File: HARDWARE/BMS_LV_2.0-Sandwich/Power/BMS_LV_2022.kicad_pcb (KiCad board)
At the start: 4 copper layers, 90 x 45 mm, 121 parts, among them J1 Conn_01x26, J11 Conn_01x07_Female, J2 AS214-97PN, J4 Battery+, J5 Battery-, J6 Conn_01x09_Female, Q1 BC846, Q10 BSS138, Q12 SIR5607DP-T1-RE3, Q13 SIR5607DP-T1-RE3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

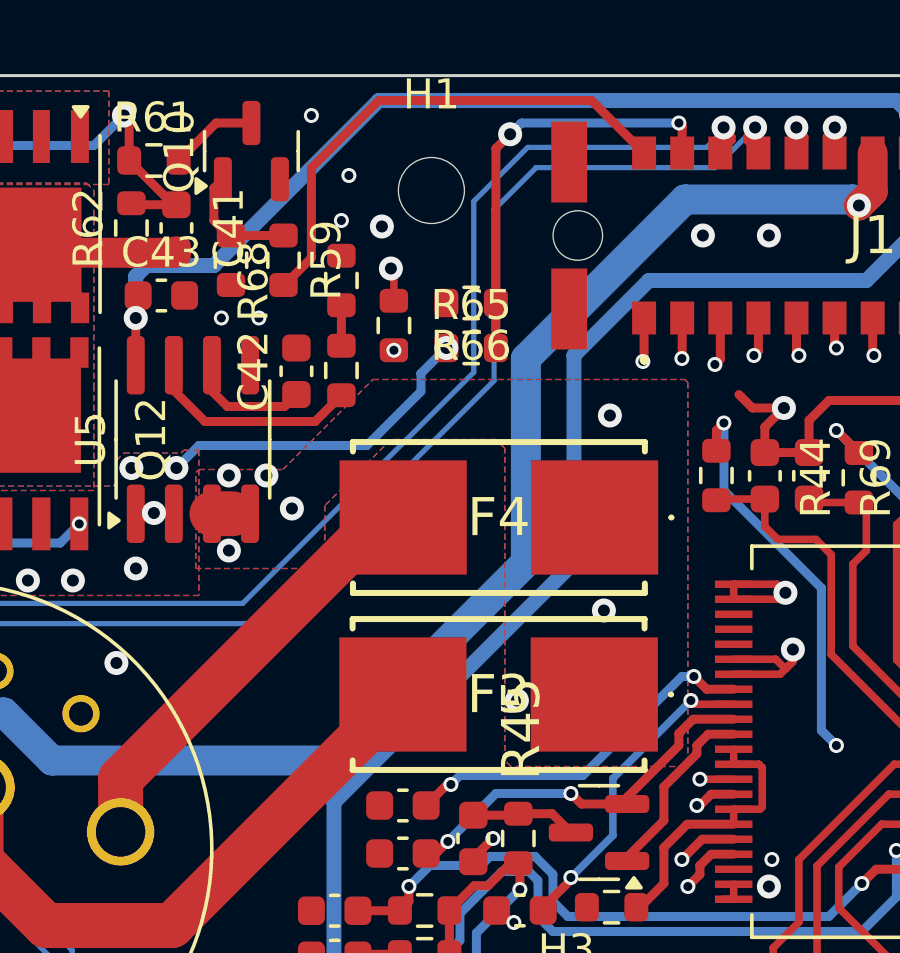
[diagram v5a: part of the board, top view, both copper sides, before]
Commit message: Przesunięto złącze do thermistorów oraz programator aby nie bylo kolizji, przesunięto tez bezpieczniki
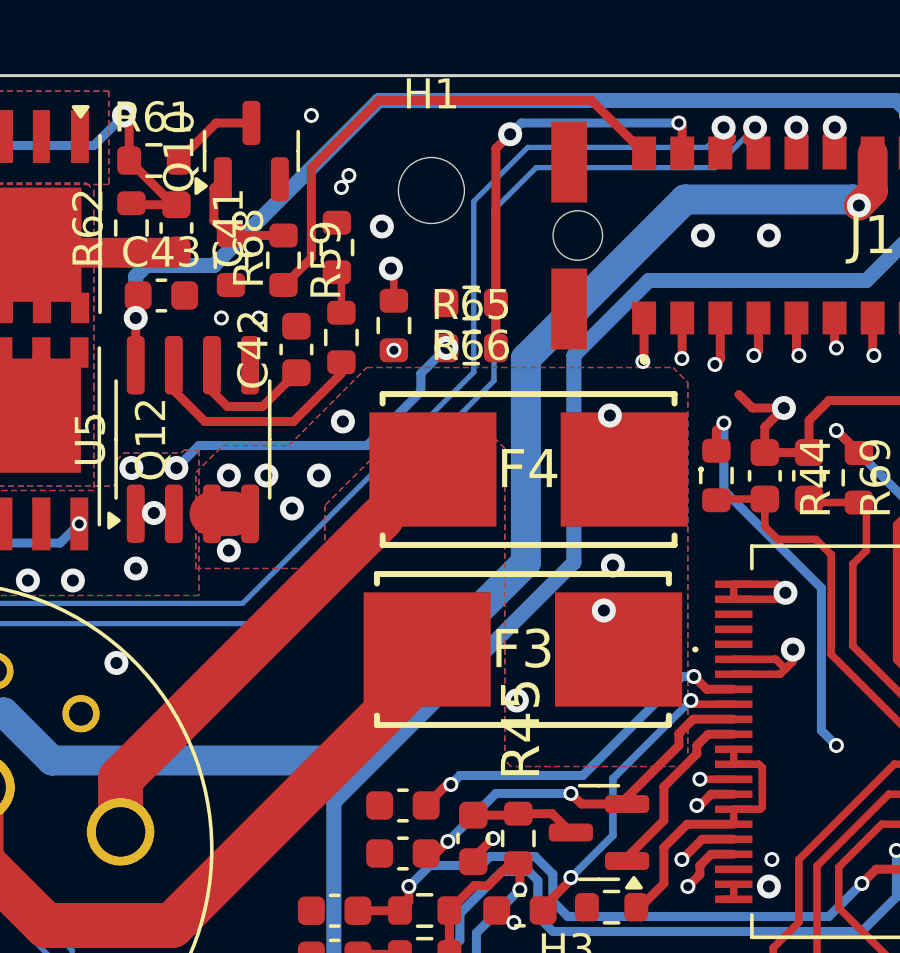
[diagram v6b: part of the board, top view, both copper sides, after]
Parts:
- moved F4 1.88 mm to (144.7, 93.1)
- moved F3 1.70 mm to (144.5, 99.1)
- moved R68 1.11 mm to (138.3, 85.7)
- moved R67 1.10 mm to (138.5, 88.7)
- moved C42 0.73 mm to (137.0, 89.1)
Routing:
- net Net-(J2-PadH): track 31.7 -> 31.0 mm
- net Net-(F3-Pad1): vias 7 -> 10
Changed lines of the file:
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@@
 	(footprint "Capacitor_SMD:C_0603_1608Metric"
 		(layer "F.Cu")
-		(at 136.967903 89.855 90)
+		(at 136.967903 89.13 90)
 		(descr "Capacitor SMD 0603 (1608 Metric), square (rectangular) end terminal, IPC-7351 nominal, (Body size source: IPC-SM-782 page 76, https://www.pcb-3d.com/wordpress/wp-content/uploads/ipc-sm-782a_amendment_1_and_2.pdf), generated with kicad-footprint-generator")
 		(tags "capacitor")
@@
 	(footprint "footprints:01550900DR"
 		(layer "F.Cu")
-		(at 143.717903 94.73 180)
+		(at 144.707903 93.13 180)
 		(descr "01550900DR-2")
 		(tags "Fuse")
@@
 	(footprint "Resistor_SMD:R_0603_1608Metric"
 		(layer "F.Cu")
-		(at 138.467903 86.83 90)
+		(at 138.317903 85.73 90)
 		(descr "Resistor SMD 0603 (1608 Metric), square (rectangular) end terminal, IPC-7351 nominal, (Body size source: IPC-SM-782 page 72, https://www.pcb-3d.com/wordpress/wp-content/uploads/ipc-sm-782a_amendment_1_and_2.pdf), generated with kicad-footprint-generator")
 		(tags "resistor")
@@
 	(footprint "footprints:01550900DR"
 		(layer "F.Cu")
-		(at 143.707904 100.63 180)
+		(at 144.517903 99.13 180)
 		(descr "01550900DR-2")
 		(tags "Fuse")
@@
 	(footprint "Resistor_SMD:R_0603_1608Metric"
 		(layer "F.Cu")
-		(at 138.467903 89.83 90)
+		(at 138.467903 88.73 90)
 		(descr "Resistor SMD 0603 (1608 Metric), square (rectangular) end terminal, IPC-7351 nominal, (Body size source: IPC-SM-782 page 72, https://www.pcb-3d.com/wordpress/wp-content/uploads/ipc-sm-782a_amendment_1_and_2.pdf), generated with kicad-footprint-generator")
 		(tags "resistor")
@@
 	)
 	(via
-		(at 138.467903 84.83)
+		(at 138.467903 83.73)
 		(size 0.5)
 		(drill 0.3)
@@
 	)
 	(segment
-		(start 136.967903 90.63)
-		(end 136.567903 91.03)
+		(start 134.667903 91.03)
+		(end 135.842903 91.03)
 		(width 0.3)
 		(layer "F.Cu")
@@
 	)
 	(segment
-		(start 134.667903 91.03)
-		(end 134.152903 90.515)
+		(start 135.842903 91.03)
+		(end 136.967903 89.905)
 		(width 0.3)
 		(layer "F.Cu")
@@
 	)
 	(segment
-		(start 134.152903 90.515)
-		(end 134.152903 89.655)
+		(start 134.152903 89.655)
+		(end 134.152903 90.515)
 		(width 0.3)
 		(layer "F.Cu")
@@
 	)
 	(segment
-		(start 136.567903 91.03)
+		(start 134.152903 90.515)
 		(end 134.667903 91.03)
 		(width 0.3)
@@
 	)
 	(via
+		(at 137.717903 93.33)
+		(size 0.8)
+		(drill 0.4)
+		(layers "F.Cu" "B.Cu")
+		(free yes)
+		(net 47)
+	)
+	(via
+		(at 138.517903 91.53)
+		(size 0.8)
+		(drill 0.4)
+		(layers "F.Cu" "B.Cu")
+		(free yes)
+		(net 47)
+	)
+	(via
 		(at 136.817903 94.43)
 		(size 0.8)
@@
 	)
 	(via
+		(at 147.517903 96.33)
+		(size 0.8)
+		(drill 0.4)
+		(layers "F.Cu" "B.Cu")
+		(free yes)
+		(net 47)
+	)
+	(via
 		(at 134.717903 93.33)
 		(size 0.8)
@@
 	)
 	(segment
-		(start 137.467903 86.08)
-		(end 136.567903 86.98)
+		(start 139.717903 80.83)
+		(end 137.467903 83.08)
 		(width 0.3)
 		(layer "F.Cu")
@@
 	)
 	(segment
-		(start 146.807903 80.83)
-		(end 139.717903 80.83)
+		(start 137.467903 83.08)
+		(end 137.467903 86.08)
 		(width 0.3)
 		(layer "F.Cu")
@@
 	)
 	(segment
-		(start 137.467903 83.08)
-		(end 137.467903 86.08)
+		(start 146.807903 80.83)
+		(end 139.717903 80.83)
 		(width 0.3)
 		(layer "F.Cu")
@@
 	)
 	(segment
-		(start 139.717903 80.83)
-		(end 137.467903 83.08)
+		(start 137.467903 86.08)
+		(end 136.567903 86.98)
 		(width 0.3)
 		(layer "F.Cu")
@@
 	)
 	(segment
-		(start 132.882903 90.495)
-		(end 133.917903 91.53)
+		(start 132.882903 89.655)
+		(end 132.882903 90.495)
 		(width 0.3)
 		(layer "F.Cu")
@@
 	)
 	(segment
-		(start 137.592903 91.53)
-		(end 138.467903 90.655)
+		(start 133.917903 91.53)
+		(end 136.867903 91.53)
 		(width 0.3)
 		(layer "F.Cu")
@@
 	)
 	(segment
-		(start 133.917903 91.53)
-		(end 137.592903 91.53)
+		(start 136.867903 91.53)
+		(end 138.467903 89.93)
 		(width 0.3)
 		(layer "F.Cu")
@@
 	)
 	(segment
-		(start 132.882903 89.655)
-		(end 132.882903 90.495)
+		(start 132.882903 90.495)
+		(end 133.917903 91.53)
 		(width 0.3)
 		(layer "F.Cu")
@@
 	)
 	(segment
-		(start 138.467903 87.655)
-		(end 138.467903 89.005)
-		(width 0.3)
+		(start 138.467903 86.705)
+		(end 138.317903 86.555)
+		(width 0.25)
+		(layer "F.Cu")
+		(net 66)
+	)
+	(segment
+		(start 138.467903 87.905)
+		(end 138.467903 86.705)
+		(width 0.25)
 		(layer "F.Cu")
 		(net 66)
@@
 	)
 	(segment
-		(start 124.517903 101.13)
-		(end 122.417903 103.23)
-		(width 0.3)
-		(layer "In2.Cu")
-		(net 81)
-	)
-	(segment
-		(start 131.317903 97.33)
-		(end 127.517903 101.13)
-		(width 0.3)
-		(layer "In2.Cu")
-		(net 81)
-	)
-	(segment
-		(start 134.467903 92.08)
-		(end 133.717903 92.83)
+		(start 122.417903 103.23)
+		(end 122.417903 105.33)
 		(width 0.3)
 		(layer "In2.Cu")
@@
 	)
 	(segment
-		(start 127.517903 101.13)
-		(end 124.517903 101.13)
+		(start 140.217903 89.155)
+		(end 137.392903 89.155)
 		(width 0.3)
 		(layer "In2.Cu")
@@
 	)
 	(segment
-		(start 140.217903 90.33)
-		(end 138.467903 92.08)
+		(start 122.417903 105.33)
+		(end 120.307903 107.44)
 		(width 0.3)
 		(layer "In2.Cu")
@@
 	)
 	(segment
-		(start 122.417903 105.33)
-		(end 120.307903 107.44)
+		(start 132.217903 97.33)
+		(end 131.317903 97.33)
 		(width 0.3)
 		(layer "In2.Cu")
@@
 	)
 	(segment
-		(start 133.717903 92.83)
-		(end 133.717903 95.83)
+		(start 120.307903 107.44)
+		(end 119.763208 107.44)
 		(width 0.3)
 		(layer "In2.Cu")
@@
 	)
 	(segment
-		(start 133.717903 95.83)
-		(end 132.217903 97.33)
+		(start 124.517903 101.13)
+		(end 122.417903 103.23)
 		(width 0.3)
 		(layer "In2.Cu")
@@
 	)
 	(segment
-		(start 140.217903 89.155)
-		(end 140.217903 90.33)
+		(start 127.517903 101.13)
+		(end 124.517903 101.13)
 		(width 0.3)
 		(layer "In2.Cu")
@@
 	)
 	(segment
-		(start 138.467903 92.08)
-		(end 134.467903 92.08)
+		(start 137.392903 89.155)
+		(end 133.717903 92.83)
 		(width 0.3)
 		(layer "In2.Cu")
@@
 	)
 	(segment
-		(start 122.417903 103.23)
-		(end 122.417903 105.33)
+		(start 133.717903 95.83)
+		(end 132.217903 97.33)
 		(width 0.3)
 		(layer "In2.Cu")
@@
 	)
 	(segment
-		(start 132.217903 97.33)
-		(end 131.317903 97.33)
+		(start 133.717903 92.83)
+		(end 133.717903 95.83)
 		(width 0.3)
 		(layer "In2.Cu")
@@
 	)
 	(segment
-		(start 120.307903 107.44)
-		(end 119.763208 107.44)
+		(start 131.317903 97.33)
+		(end 127.517903 101.13)
 		(width 0.3)
 		(layer "In2.Cu")
@@
 		(polygon
 			(pts
-				(xy 133.717903 93.13) (xy 136.517903 93.13) (xy 139.517903 90.13) (xy 149.917903 90.13) (xy 150.017903 90.23)
+				(xy 134.517903 92.33) (xy 136.717903 92.33) (xy 139.317903 89.73) (xy 149.517903 89.73) (xy 150.017903 90.23)
 				(xy 150.017903 102.93) (xy 149.917903 103.03) (xy 144.117903 103.03) (xy 143.917903 102.83) (xy 143.917903 92.43)
 				(xy 143.617903 92.13) (xy 140.117903 92.13) (xy 137.917903 94.33) (xy 137.917903 95.83) (xy 137.317903 96.43)

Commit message: Kolejna kurwa wersja gotowa, japierdole
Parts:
- removed C25, C26, C27, C28, C29, C30, C45, C46: 100nF, Capacitor_SMD:C_0603_1608Metric
- removed D1: D_Zener_Small, Diode_SMD:D_0805_2012Metric_Pad1.15x1.40mm_HandSolder
- removed J6: Conn_01x09_Female, Connector_JST:JST_XH_B9B-XH-A_1x09_P2.50mm_Vertical
- removed R51, R52, R53, R54, R55, R56, R63, R64: 10k, Resistor_SMD:R_0603_1608Metric
- removed R72: 100, Resistor_SMD:R_0603_1608Metric
- moved F3 0.49 mm to (144.0, 99.1)
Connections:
- F1 pad 2: +24V -> VCC
- J1 pad 10: /Therm_6 -> unconnected-(J1-Pin_10-Pad10)
- J1 pad 11: /Therm_7 -> unconnected-(J1-Pin_11-Pad11)
- J1 pad 12: /Therm_8 -> unconnected-(J1-Pin_12-Pad12)
- J1 pad 5: /Therm_1 -> unconnected-(J1-Pin_5-Pad5)
- J1 pad 6: /Therm_2 -> unconnected-(J1-Pin_6-Pad6)
- J1 pad 7: /Therm_3 -> unconnected-(J1-Pin_7-Pad7)
- J1 pad 8: /Therm_4 -> unconnected-(J1-Pin_8-Pad8)
- J1 pad 9: /Therm_5 -> unconnected-(J1-Pin_9-Pad9)
- J4 pad 1: +24V -> VCC
- Q13 pad 2: +24V -> VCC
- Q15 pad 2: +24V -> VCC
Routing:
- net /Thermistors/3V3_zener: track 48.4 -> 0.00 mm, vias 8 -> 0
- net +3V3: track 47.6 -> 0.00 mm, vias 2 -> 0
- net /Therm_7: track 45.7 -> 0.00 mm, vias 2 -> 0
- net /Therm_8: track 44.8 -> 0.00 mm, vias 2 -> 0
- net /Therm_6: track 42.7 -> 0.00 mm, vias 2 -> 0
- net /Therm_4: track 40.1 -> 0.00 mm, vias 2 -> 0
- net /Therm_5: track 40.0 -> 0.00 mm, vias 2 -> 0
- net /Therm_1: track 37.8 -> 0.00 mm, vias 2 -> 0
- net /Therm_3: track 37.6 -> 0.00 mm, vias 2 -> 0
- net /Therm_2: track 36.9 -> 0.00 mm, vias 2 -> 0
- net VCC: track 47.7 -> 54.6 mm, vias 1 -> 48
- net /LTC6810/CellBalance6: track 112.8 -> 111.5 mm
- net /eFuse/Gate: track 43.6 -> 42.8 mm
- net +24V: vias 47 -> 0
- added copper zone on B.Cu, net VCC
- added copper zone on F.Cu, net VCC
- added copper zone on In1.Cu, net VCC
- added copper zone on In2.Cu, net VCC
- removed copper zone on B.Cu, net +24V
- removed copper zone on F.Cu, net +24V
- removed copper zone on In1.Cu, net +24V
- removed copper zone on In2.Cu, net +24V
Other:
- board text removed: "GND"
- board text removed: "Therm_1"

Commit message: Ulozono silkscreena
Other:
- board text added: "B6,B5,B4,B3,B2,B1"
- board text added: "BMS LV POWER 2026"
- board text added: "BMS SANDWICH 2026 By Wiktor Krakowski V2.0 :P"
- board text added: "CH1 ON"
- board text added: "CH2 ON"
- board text added: "Look UP!"
- board text removed: "2024"
- board text removed: "FUSE 1 OK"
- board text removed: "FUSE 2 OK"
